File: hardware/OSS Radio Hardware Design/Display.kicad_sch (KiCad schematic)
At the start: 19 parts, among them J3 Display_Connector-0.5mmZIF-AE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, Q1 Si1308EDL

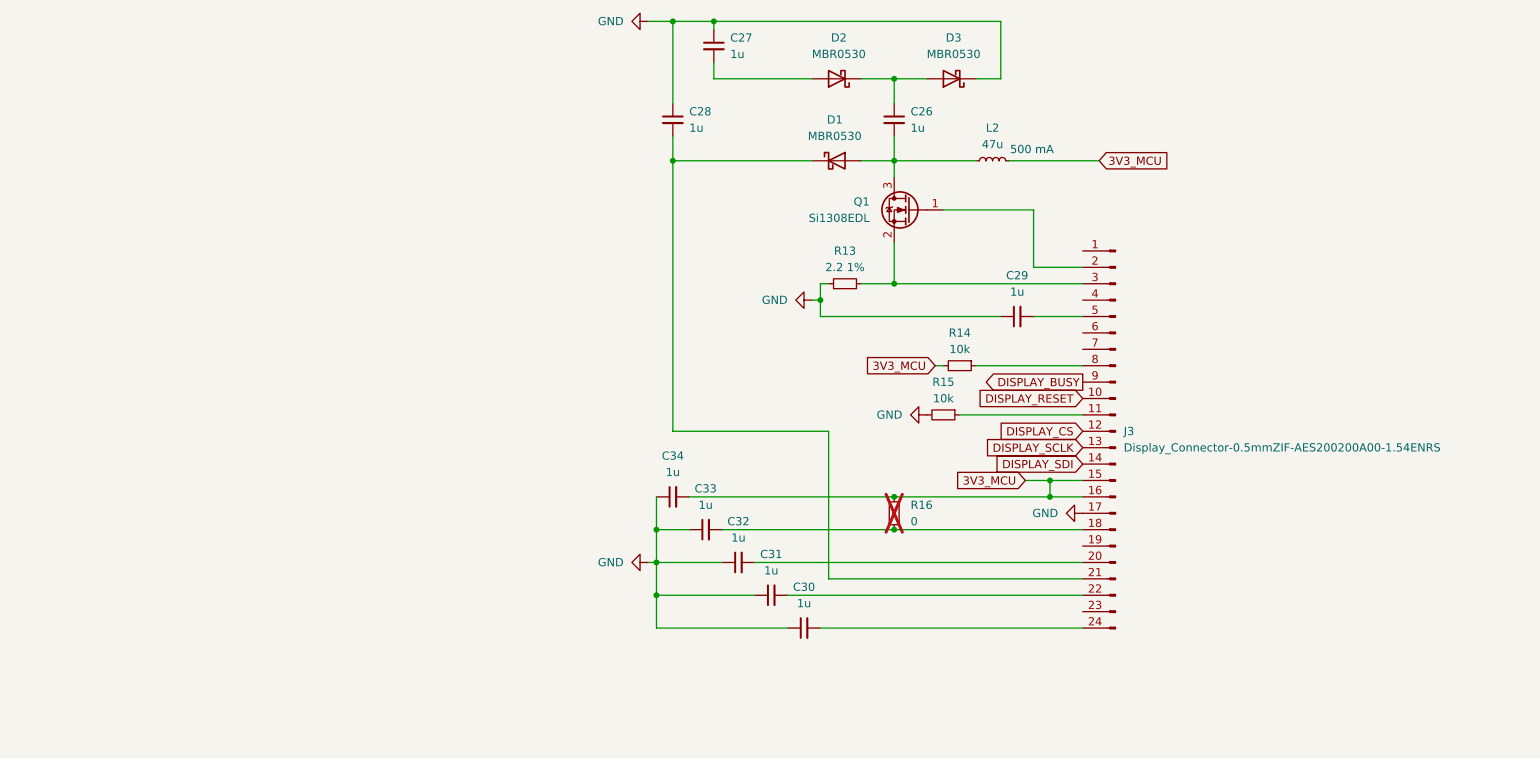
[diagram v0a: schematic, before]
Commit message: schematic for sd card, external flash, working on audio amp
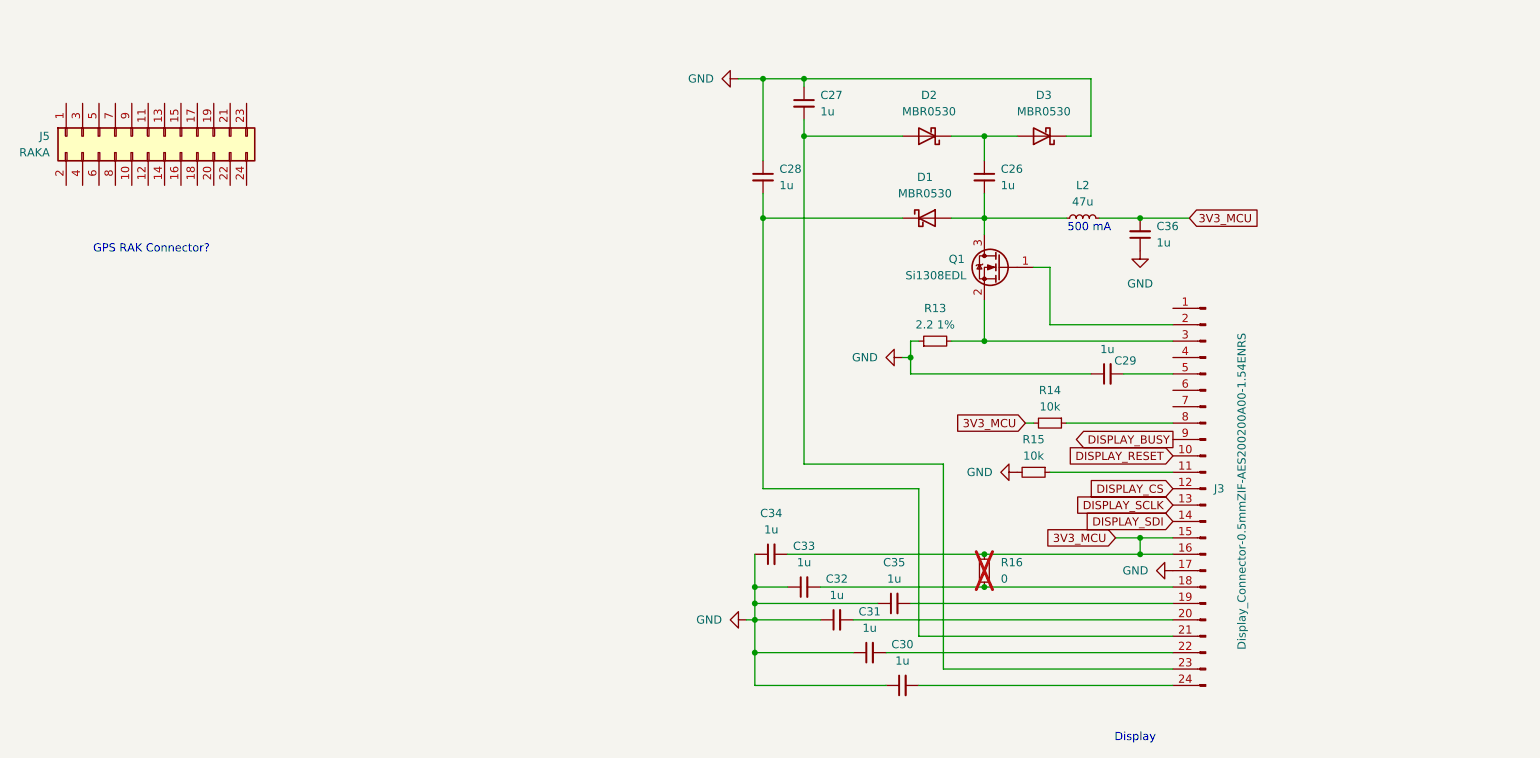
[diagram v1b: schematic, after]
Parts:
- added C35, C36: 1u, symbol Device:C_Small
- added J5: RAKA, symbol Connector_Generic:Conn_02x12_Odd_Even
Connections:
- net 3V3_MCU: now also C36.2
- net GND: now also C35.1, C36.1
- net at C27.2, D2.2 (A): now also J3.23 (Pin_23)
- net at J3.19 (Pin_19): now also C35.2
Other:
- note added: "Display"
- note added: "GPS RAK Connector?"
- moved on the sheet: C26, C27, C28, C29, C30, C31, C32, C33, C34, D1, D2, D3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

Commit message: working on battery protection and charge
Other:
- note added: "Need to re-select FET for BOM. Check to see if AO4300A works"
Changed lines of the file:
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@@
 	(generator_version "9.0")
 	(paper "A4")
+	(text "Need to re-select FET for BOM. Check to see if AO4300A works"
+		(exclude_from_sim no)
+		(at 126.238 94.234 0)
+		(effects
+			(font
+				(size 1.27 1.27)
+			)
+		)
+	)
 	(text "GPS RAK Connector?\n"
 		(exclude_from_sim no)

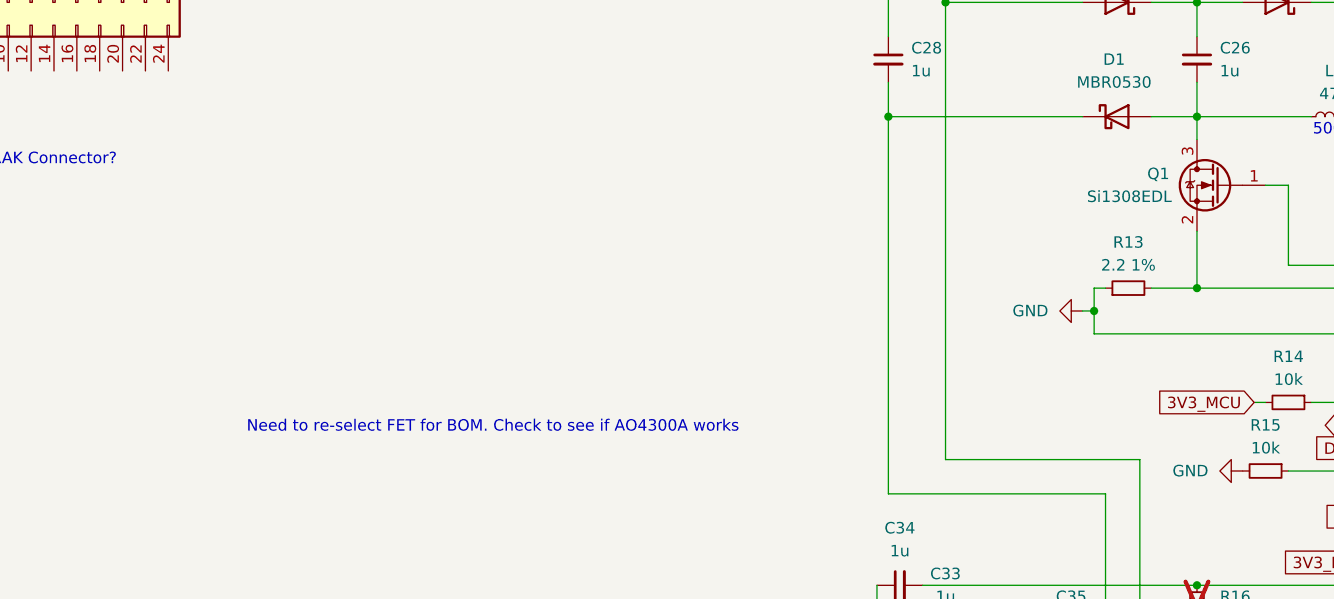
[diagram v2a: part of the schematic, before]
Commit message: finished battery and charger. Now all i need is RF output stages, GPS, and Buttons
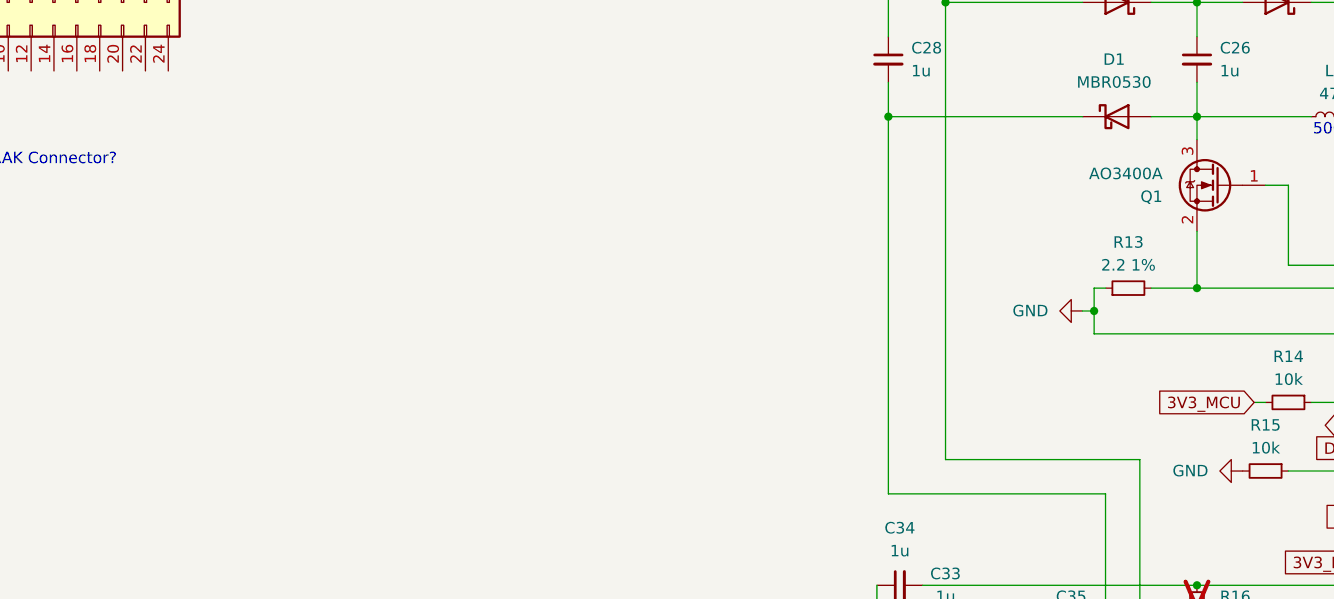
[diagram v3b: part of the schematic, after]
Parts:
- removed Q1: Si1308EDL, Package_TO_SOT_SMD:SOT-323_SC-70, symbol Transistor_FET:Si1308EDL
- added Q1: AO3400A, Package_TO_SOT_SMD:SOT-23, symbol Transistor_FET:AO3400A
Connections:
- net at J3.2 (Pin_2): now also Q1.1 (G)
- net at J3.3 (Pin_3), R13.2: now also Q1.2 (S)
- net at C26.2, D1.2 (A), L2.1: now also Q1.3 (D)
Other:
- note removed: "Need to re-select FET for BOM. Check to see if AO4300A works"

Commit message: working on fooprints
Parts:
- C26, C27, C28, C29, C30, C31, C32, C33, C34, C35, C36: footprint (none) -> Capacitor_SMD:C_0603_1608Metric_Pad1.08x0.95mm_HandSolder
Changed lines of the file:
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@@
 			)
 		)
-		(property "Footprint" ""
+		(property "Footprint" "Capacitor_SMD:C_0603_1608Metric_Pad1.08x0.95mm_HandSolder"
 			(at 176.53 116.84 0)
 			(effects
@@
 			)
 		)
-		(property "Footprint" ""
+		(property "Footprint" "Capacitor_SMD:C_0603_1608Metric_Pad1.08x0.95mm_HandSolder"
 			(at 171.45 111.76 0)
 			(effects
@@
 			)
 		)
-		(property "Footprint" ""
+		(property "Footprint" "Capacitor_SMD:C_0603_1608Metric_Pad1.08x0.95mm_HandSolder"
 			(at 191.77 132.08 0)
 			(effects
@@
 			)
 		)
-		(property "Footprint" ""
+		(property "Footprint" "Capacitor_SMD:C_0603_1608Metric_Pad1.08x0.95mm_HandSolder"
 			(at 181.61 121.92 0)
 			(effects
@@
 			)
 		)
-		(property "Footprint" ""
+		(property "Footprint" "Capacitor_SMD:C_0603_1608Metric_Pad1.08x0.95mm_HandSolder"
 			(at 190.5 119.38 0)
 			(effects
@@
 			)
 		)
-		(property "Footprint" ""
+		(property "Footprint" "Capacitor_SMD:C_0603_1608Metric_Pad1.08x0.95mm_HandSolder"
 			(at 186.69 127 0)
 			(effects
@@
 			)
 		)
-		(property "Footprint" ""
+		(property "Footprint" "Capacitor_SMD:C_0603_1608Metric_Pad1.08x0.95mm_HandSolder"
 			(at 170.18 53.34 0)
 			(effects
@@
 			)
 		)
-		(property "Footprint" ""
+		(property "Footprint" "Capacitor_SMD:C_0603_1608Metric_Pad1.08x0.95mm_HandSolder"
 			(at 176.53 41.91 0)
 			(effects
@@
 			)
 		)
-		(property "Footprint" ""
+		(property "Footprint" "Capacitor_SMD:C_0603_1608Metric_Pad1.08x0.95mm_HandSolder"
 			(at 223.52 83.82 0)
 			(effects
@@
 			)
 		)
-		(property "Footprint" ""
+		(property "Footprint" "Capacitor_SMD:C_0603_1608Metric_Pad1.08x0.95mm_HandSolder"
 			(at 204.47 53.34 0)
 			(effects
@@
 			)
 		)
-		(property "Footprint" ""
+		(property "Footprint" "Capacitor_SMD:C_0603_1608Metric_Pad1.08x0.95mm_HandSolder"
 			(at 228.6 62.23 0)
 			(effects
